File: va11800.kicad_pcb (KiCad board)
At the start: 2 copper layers, 389.5 x 166.4 mm, 255 parts, among them J1 Conn_01x16_Female, J2 Conn_01x16_Female, j1 MX-NoLED, k1 MX-NoLED, m1 MX-NoLED, p1 MX-NoLED, q1 MX-NoLED, t1 MX-NoLED, u1 MX-NoLED, x1 MX-NoLED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

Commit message: rename project and small silkscreen adjustments
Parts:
- added Kicad: KiCad-Logo2_5mm_SilkScreen, Symbol:KiCad-Logo2_5mm_SilkScreen, B.Cu at (272.8, 64.0)
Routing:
- net GND: track 493.1 -> 501.0 mm
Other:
- board text added: "02/2022"
- board text added: "VA11800 V1.0"
- board text added: "https://github.com/vuckale"

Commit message: fix footprint associations
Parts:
- D17, D50, D52: footprint Keebio-Parts:LED_D2.00mm -> vuckale:LED_D2.00mm

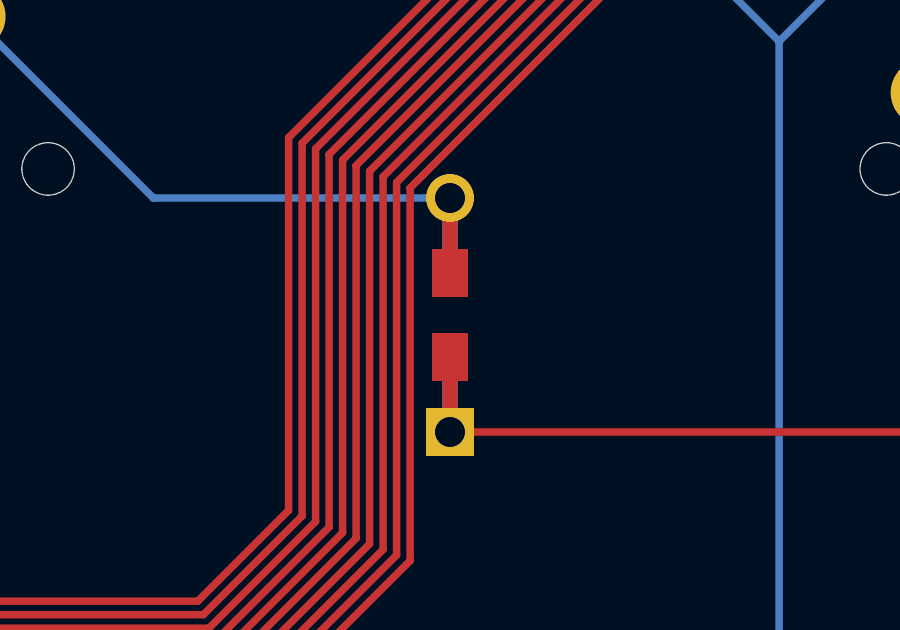
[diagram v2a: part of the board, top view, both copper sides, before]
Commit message: add github repository silkscreen
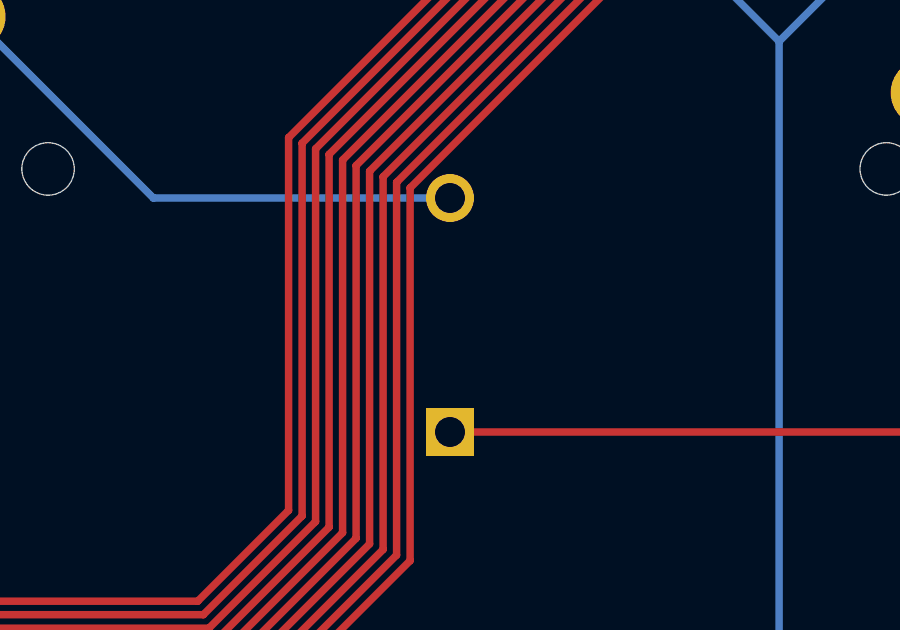
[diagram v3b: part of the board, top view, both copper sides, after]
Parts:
- D1: footprint Keebio-Parts:Diode-dual -> vuckale:Diode
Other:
- board text added: "https://github.com/vuckale/va11800-pcb"

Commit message: add silkscreen on traces
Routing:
- net GND: track 501.0 -> 508.1 mm
- net col6: track 540.5 -> 546.5 mm
- net col7: track 597.3 -> 592.8 mm
- net col5: track 431.9 -> 435.6 mm
- net Net-(D74-Pad2): track 35.2 -> 33.1 mm
- net row12: track 796.5 -> 795.3 mm
- net col4: track 552.2 -> 551.0 mm

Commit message: small logo adjustments
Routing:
- net row12: track 795.3 -> 775.1 mm
- net row2: track 383.4 -> 378.4 mm
- net row0: track 507.4 -> 502.7 mm
- net row13: track 839.2 -> 839.9 mm

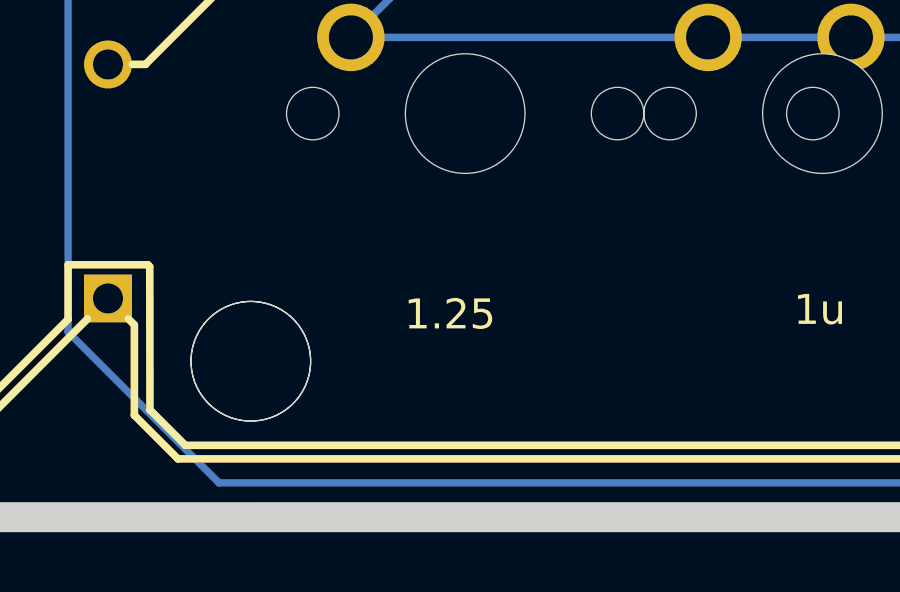
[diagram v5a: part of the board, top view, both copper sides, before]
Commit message: add missing letter "u" for bottom row
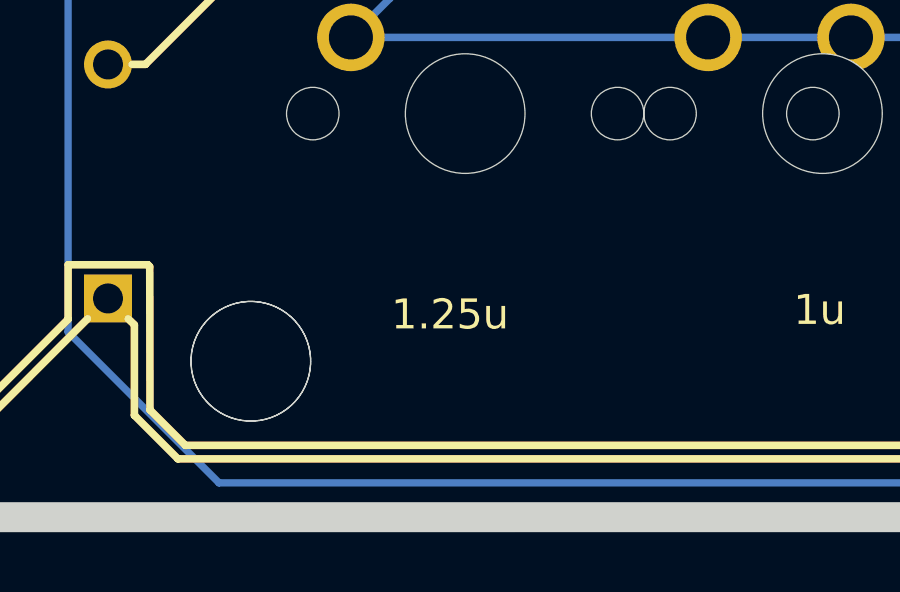
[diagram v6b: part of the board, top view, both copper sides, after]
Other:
- board text removed: "1.25"
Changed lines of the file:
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@@
     (effects (font (size 1 1) (thickness 0.15)))
   )
-  (gr_text 1.25 (at 206.66 219.1) (layer F.SilkS)
+  (gr_text 1.25u (at 206.66 219.1) (layer F.SilkS)
     (effects (font (size 1 1) (thickness 0.15)))
   )
